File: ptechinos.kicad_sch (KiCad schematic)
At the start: 59 parts, among them J1 Bat_Pos, J2 Battery, J3 Bat_GND, J4 AudioJack4, SW1 SW_Power, SW2 Reset, U1 ProMicro

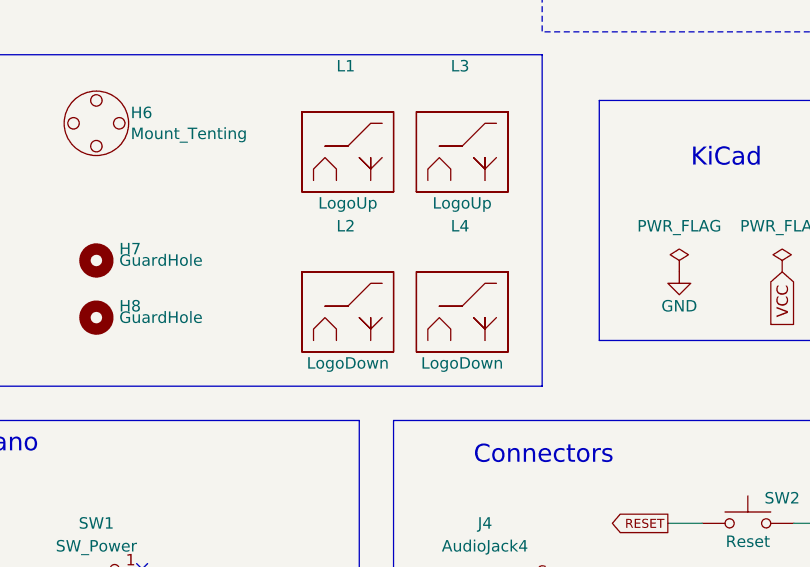
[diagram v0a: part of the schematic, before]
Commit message: ♻️ - Update PCB with new graphics. Create a light version of tenting puck with less details (silkscreen, ...). Bump to V0.3
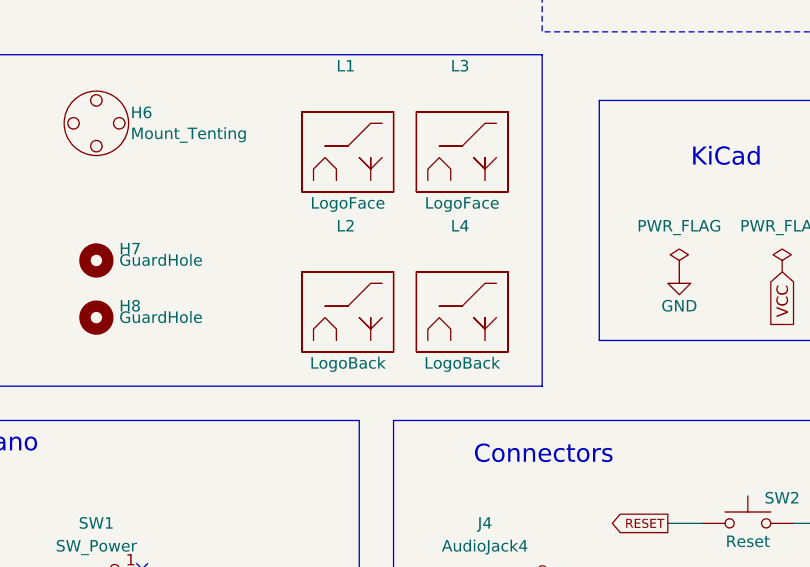
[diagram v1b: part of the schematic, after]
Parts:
- H6: footprint ptechinos:Tenting_Puck -> ptechinos:Tenting_Puck_soft
- L1: value LogoUp -> LogoFace
- L2: value LogoDown -> LogoBack; footprint ptechinos:pterodactyl-medium -> ptechinos:hedgehog-medium
- L3: value LogoUp -> LogoFace; footprint ptechinos:hedgehog-medium_back -> ptechinos:pterodactyl-medium
- L4: value LogoDown -> LogoBack; footprint ptechinos:pterodactyl-medium_back -> ptechinos:pterodactyl-medium
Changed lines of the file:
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@@
     (title "Ptechinos")
     (date "2022-04-16")
-    (rev "0.2")
+    (rev "0.3")
     (comment 1 "A crossover between Pteron36 and Balbuzard.")
   )
@@
       (effects (font (size 1.27 1.27)) (justify left))
     )
-    (property "Value" "LogoDown" (id 1) (at 105.41 151.13 0))
-    (property "Footprint" "ptechinos:pterodactyl-medium" (id 2) (at 105.41 153.67 0)
+    (property "Value" "LogoBack" (id 1) (at 105.41 151.13 0))
+    (property "Footprint" "ptechinos:hedgehog-medium" (id 2) (at 105.41 153.67 0)
       (effects (font (size 1.27 1.27)) hide)
     )
@@
       (effects (font (size 1.27 1.27)) (justify left))
     )
-    (property "Value" "LogoUp" (id 1) (at 105.41 133.35 0))
+    (property "Value" "LogoFace" (id 1) (at 105.41 133.35 0))
     (property "Footprint" "ptechinos:hedgehog-medium" (id 2) (at 105.41 135.89 0)
       (effects (font (size 1.27 1.27)) hide)
@@
       (effects (font (size 1.27 1.27)) (justify left))
     )
-    (property "Value" "LogoUp" (id 1) (at 118.11 133.35 0))
-    (property "Footprint" "ptechinos:hedgehog-medium_back" (id 2) (at 118.11 135.89 0)
+    (property "Value" "LogoFace" (id 1) (at 118.11 133.35 0))
+    (property "Footprint" "ptechinos:pterodactyl-medium" (id 2) (at 118.11 135.89 0)
       (effects (font (size 1.27 1.27)) hide)
     )
@@
       (effects (font (size 1.27 1.27)) (justify left bottom))
     )
-    (property "Footprint" "ptechinos:Tenting_Puck" (id 2) (at 77.47 124.46 0)
+    (property "Footprint" "ptechinos:Tenting_Puck_soft" (id 2) (at 77.47 124.46 0)
       (effects (font (size 1.27 1.27)) hide)
     )
@@
       (effects (font (size 1.27 1.27)) (justify left))
     )
-    (property "Value" "LogoDown" (id 1) (at 118.11 151.13 0))
-    (property "Footprint" "ptechinos:pterodactyl-medium_back" (id 2) (at 118.11 153.67 0)
+    (property "Value" "LogoBack" (id 1) (at 118.11 151.13 0))
+    (property "Footprint" "ptechinos:pterodactyl-medium" (id 2) (at 118.11 153.67 0)
       (effects (font (size 1.27 1.27)) hide)
     )
@@
     )
     (path "/d98b06b1-d759-4372-889f-6ac21114139f"
-      (reference "H6") (unit 1) (value "Mount_Tenting") (footprint "ptechinos:Tenting_Puck")
+      (reference "H6") (unit 1) (value "Mount_Tenting") (footprint "ptechinos:Tenting_Puck_soft")
     )
     (path "/fb635d95-7100-4c05-a33e-7d995a9dd129"
@@
     )
     (path "/3ac0cb69-9e9e-4031-b1b5-abf5b4e1cd57"
-      (reference "L1") (unit 1) (value "LogoUp") (footprint "ptechinos:hedgehog-medium")
+      (reference "L1") (unit 1) (value "LogoFace") (footprint "ptechinos:hedgehog-medium")
     )
     (path "/00259991-bdab-444e-a6e2-c9dca6e952c5"
-      (reference "L2") (unit 1) (value "LogoDown") (footprint "ptechinos:pterodactyl-medium")
+      (reference "L2") (unit 1) (value "LogoBack") (footprint "ptechinos:hedgehog-medium")
     )
     (path "/bc1145e9-b65b-4d7f-95dd-5d9104e32147"
-      (reference "L3") (unit 1) (value "LogoUp") (footprint "ptechinos:hedgehog-medium_back")
+      (reference "L3") (unit 1) (value "LogoFace") (footprint "ptechinos:pterodactyl-medium")
     )
     (path "/fe38f860-b64c-4cd4-b25a-0eab509d1952"
-      (reference "L4") (unit 1) (value "LogoDown") (footprint "ptechinos:pterodactyl-medium_back")
+      (reference "L4") (unit 1) (value "LogoBack") (footprint "ptechinos:pterodactyl-medium")
     )
     (path "/002c56c8-3b30-4e32-9e35-0b9ffbae1671"

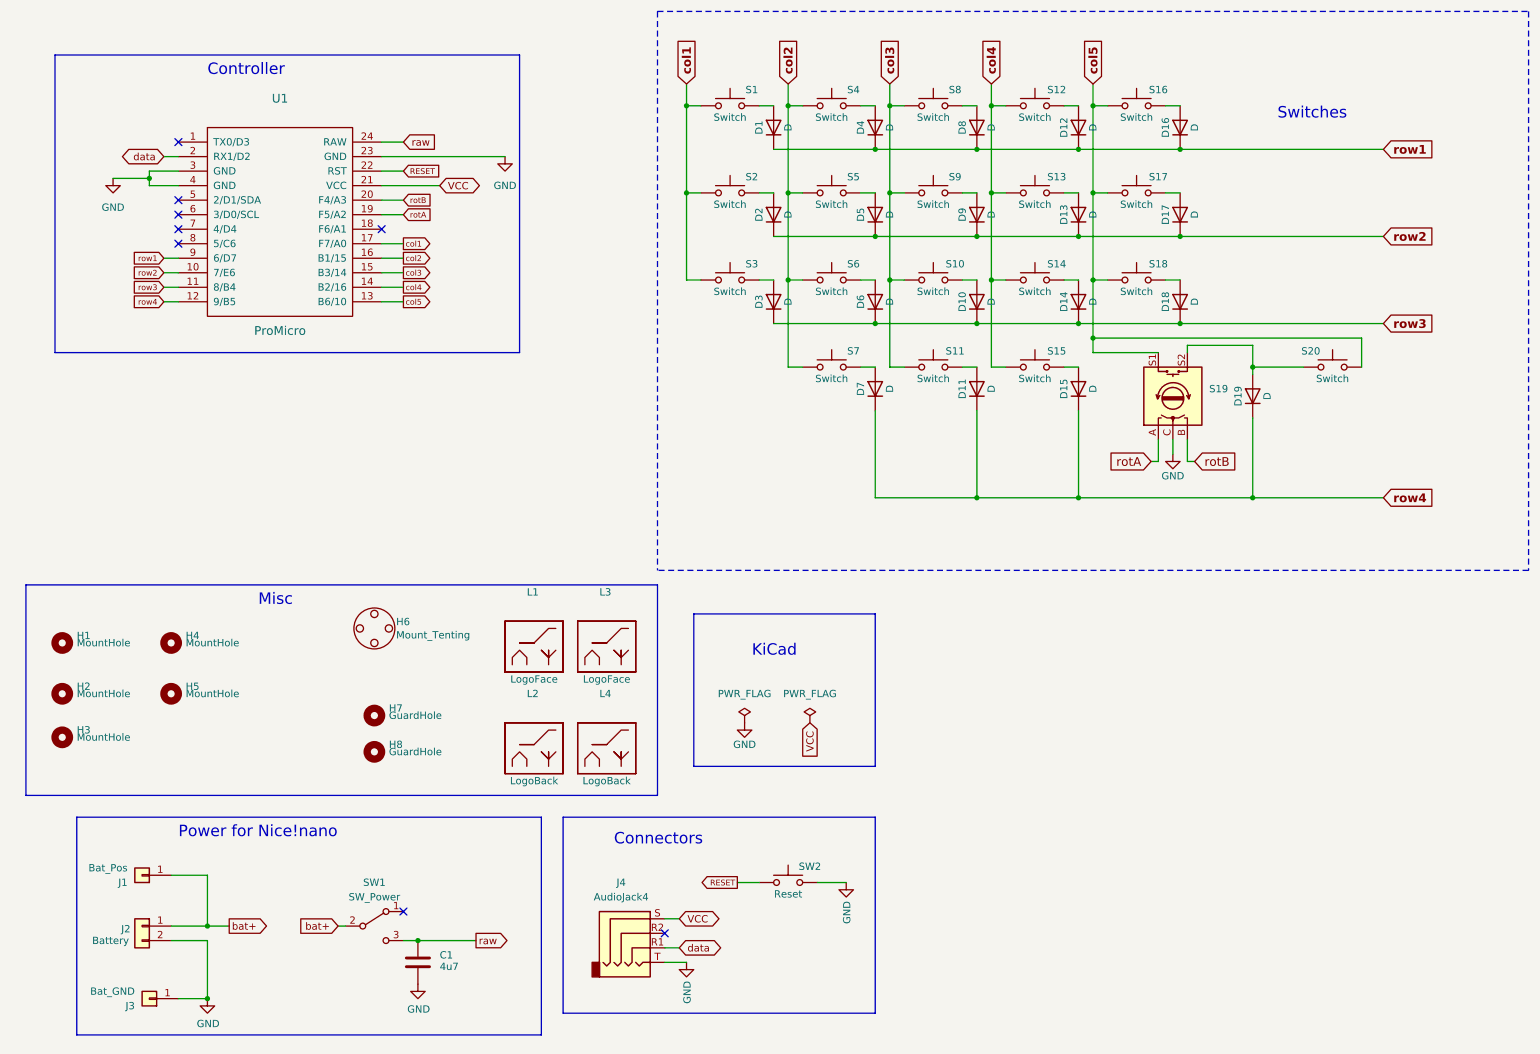
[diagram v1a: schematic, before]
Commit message: ♻️ - Better naming convention for logos.
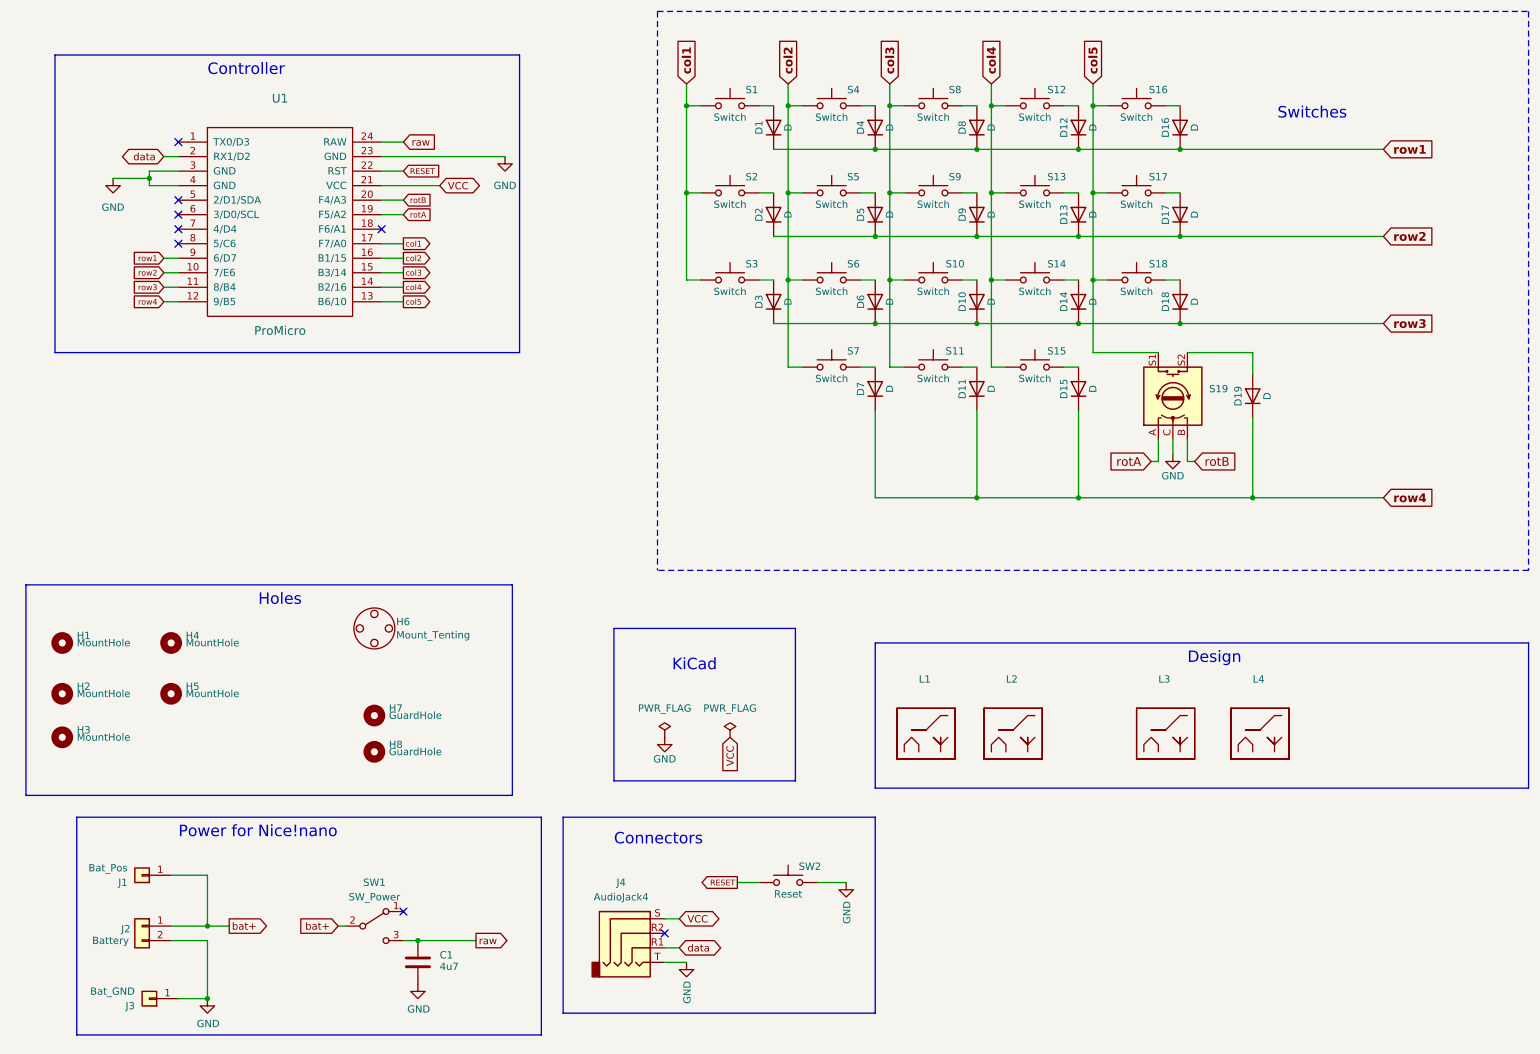
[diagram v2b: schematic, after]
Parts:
- removed S20: Switch, ptechinos:pg1350-R, symbol Switch:SW_Push
- L1: value LogoFace -> (none); footprint ptechinos:hedgehog-medium -> (none)
- L2: value LogoBack -> (none); footprint ptechinos:hedgehog-medium -> (none)
- L3: value LogoFace -> (none); footprint ptechinos:pterodactyl-medium -> (none)
- L4: value LogoBack -> (none); footprint ptechinos:pterodactyl-medium -> (none)
- S19: footprint ptechinos:RollerEncoder_Panasonic_EVQWGD001 -> ptechinos:pg1350-EVQWGD001_R
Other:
- note added: "Design"
- note added: "Holes"
- note removed: "Misc"

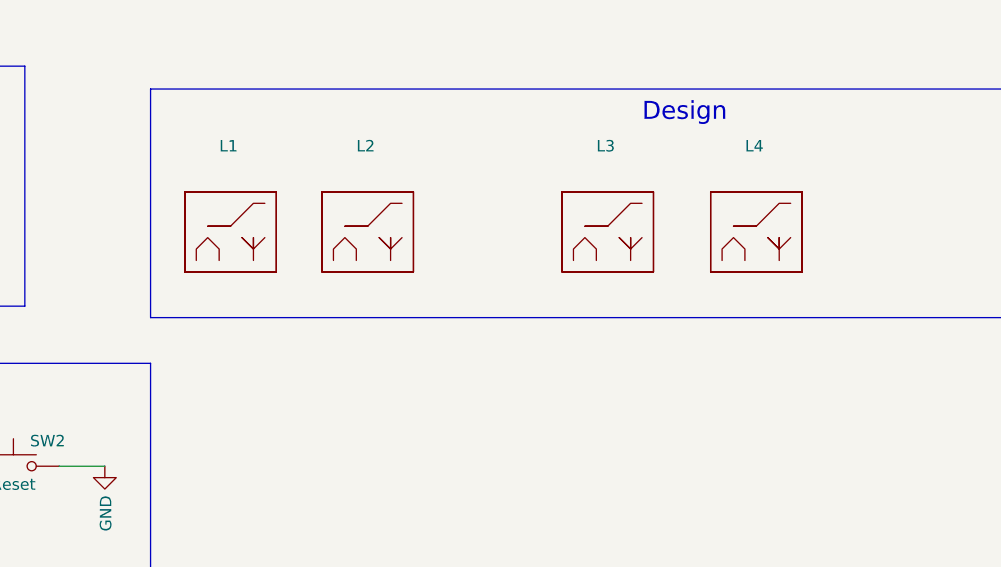
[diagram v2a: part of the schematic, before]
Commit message: ♻️ ✨ - More descriptive logo names (schema). Add board name to PCB.
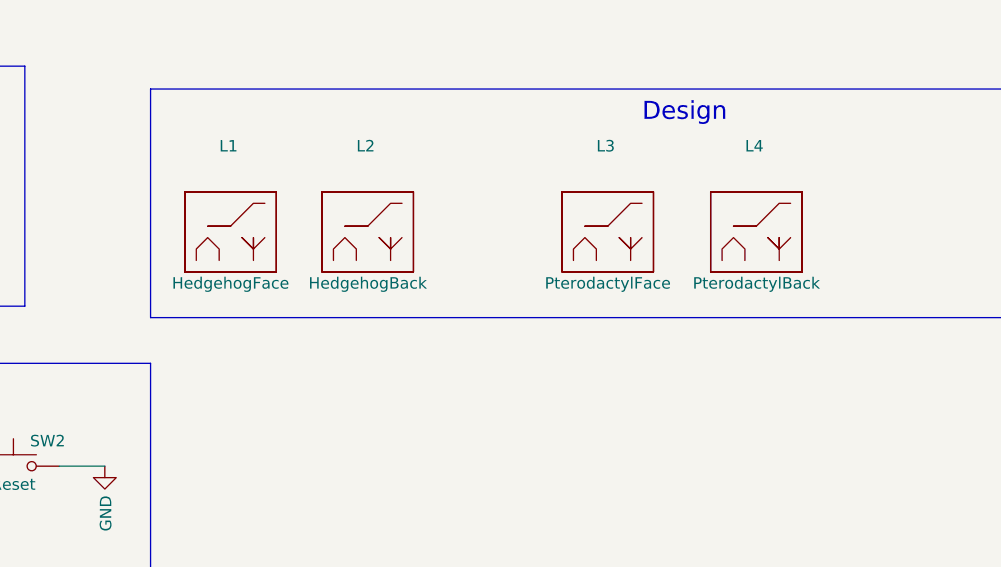
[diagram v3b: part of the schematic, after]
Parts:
- L1: value (none) -> HedgehogFace; footprint (none) -> ptechinos:hedgehog-medium
- L2: value (none) -> HedgehogBack; footprint (none) -> ptechinos:hedgehog-medium
- L3: value (none) -> PterodactylFace; footprint (none) -> ptechinos:pterodactyl-medium
- L4: value (none) -> PterodactylBack; footprint (none) -> ptechinos:pterodactyl-medium
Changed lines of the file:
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@@
   (title_block
     (title "Ptechinos")
-    (date "2022-04-16")
-    (rev "0.3")
+    (date "2022-05-06")
+    (rev "0.4")
     (comment 1 "A crossover between Pteron36 and Balbuzard.")
   )
@@
       (effects (font (size 1.27 1.27)) (justify left))
     )
-    (property "Value" "" (id 1) (at 189.23 148.59 0))
-    (property "Footprint" "" (id 2) (at 189.23 151.13 0)
+    (property "Value" "HedgehogBack" (id 1) (at 189.23 148.59 0))
+    (property "Footprint" "ptechinos:hedgehog-medium" (id 2) (at 189.23 151.13 0)
       (effects (font (size 1.27 1.27)) hide)
     )
@@
       (effects (font (size 1.27 1.27)) (justify left))
     )
-    (property "Value" "" (id 1) (at 232.41 148.59 0))
-    (property "Footprint" "" (id 2) (at 232.41 151.13 0)
+    (property "Value" "PterodactylBack" (id 1) (at 232.41 148.59 0))
+    (property "Footprint" "ptechinos:pterodactyl-medium" (id 2) (at 232.41 151.13 0)
       (effects (font (size 1.27 1.27)) hide)
     )
@@
       (effects (font (size 1.27 1.27)) (justify left))
     )
-    (property "Value" "" (id 1) (at 215.9 148.59 0))
-    (property "Footprint" "" (id 2) (at 215.9 151.13 0)
+    (property "Value" "PterodactylFace" (id 1) (at 215.9 148.59 0))
+    (property "Footprint" "ptechinos:pterodactyl-medium" (id 2) (at 215.9 151.13 0)
       (effects (font (size 1.27 1.27)) hide)
     )
@@
       (effects (font (size 1.27 1.27)) (justify left))
     )
-    (property "Value" "" (id 1) (at 173.99 148.59 0))
-    (property "Footprint" "" (id 2) (at 173.99 151.13 0)
-      (effects (font (size 1.27 1.27)) hide)
-    )
+    (property "Value" "HedgehogFace" (id 1) (at 173.99 148.59 0))
+    (property "Footprint" "ptechinos:hedgehog-medium" (id 2) (at 173.99 151.13 0)
+      (effects (font (size 1.27 1.27)) hide)
+    )
